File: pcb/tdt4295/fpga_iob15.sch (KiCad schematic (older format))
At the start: 18 parts

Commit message: add another capacitor :)
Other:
- note added: "Have SPIs between FPGA and MCU on IOB15?"
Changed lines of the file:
@@
 Text Notes 4300 2550 2    50   ~ 0
 Datasheet says:\n1x47uF\n2x4.7uF\n4x470nF
+Text Notes 4650 3400 2    50   ~ 10
+Have SPIs between FPGA and MCU on IOB15?
 $EndSCHEMATC

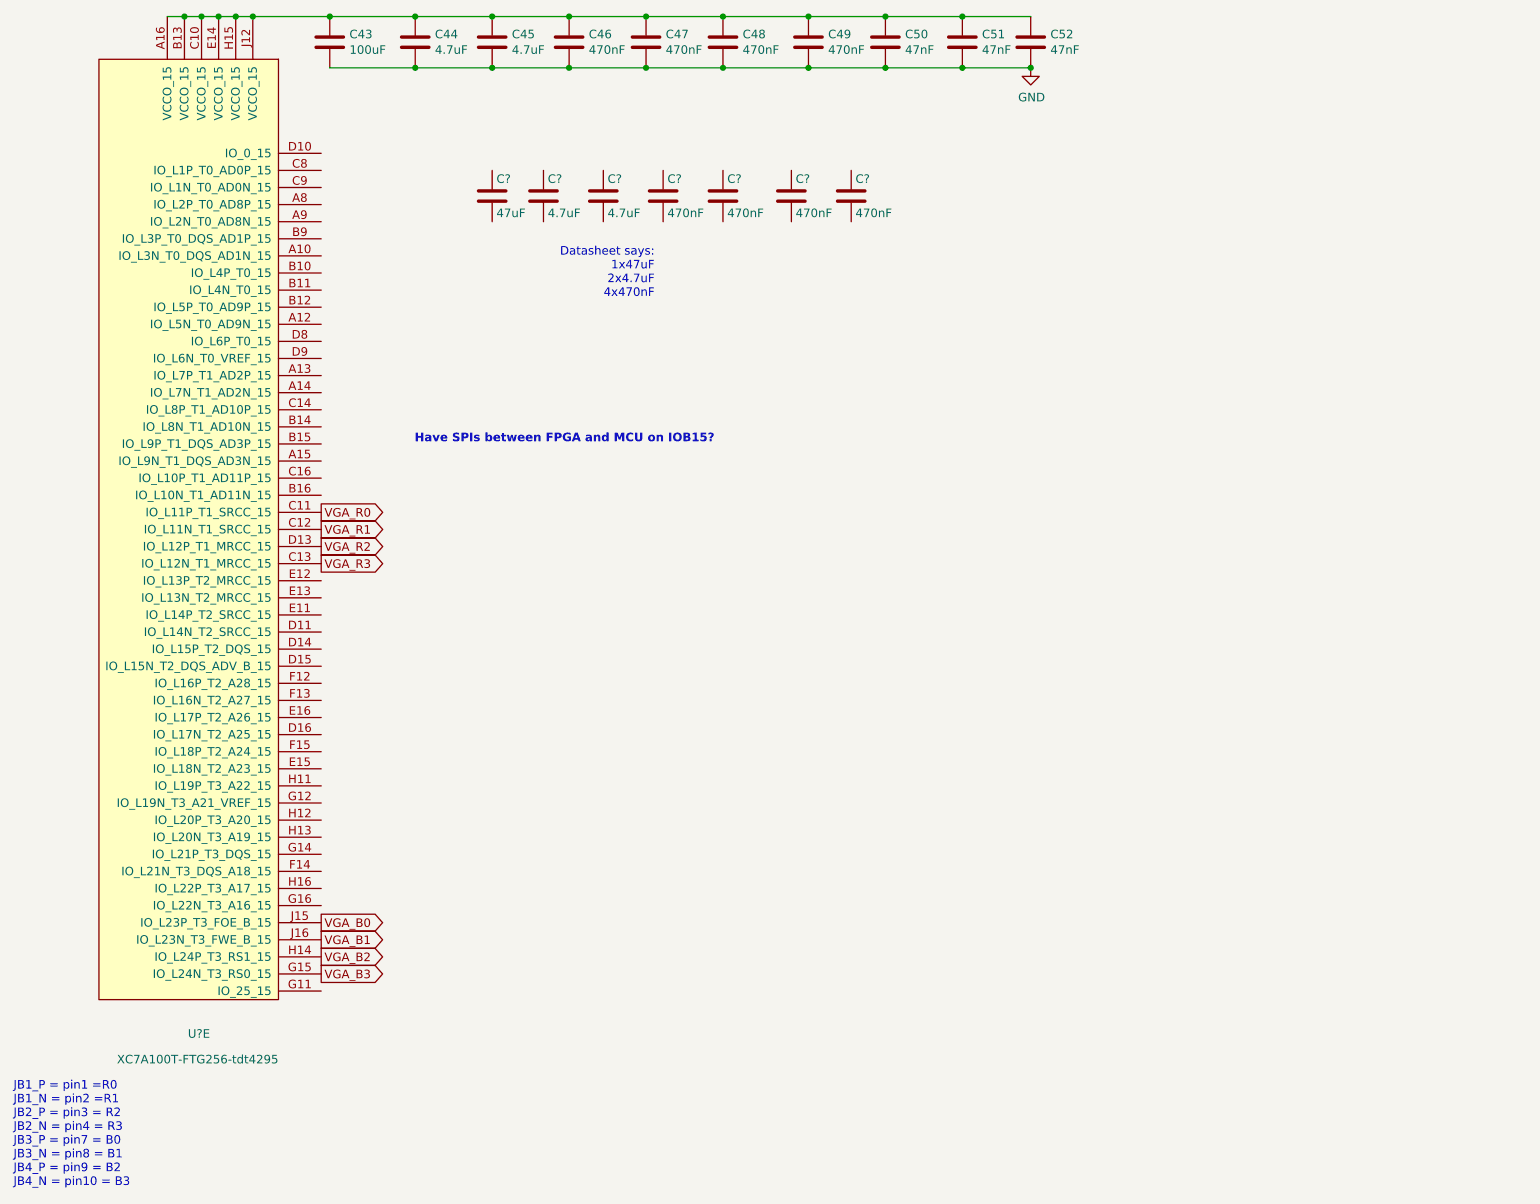
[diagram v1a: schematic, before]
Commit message: Add digikey footprints, implement (some) capacitor footprints in schematic
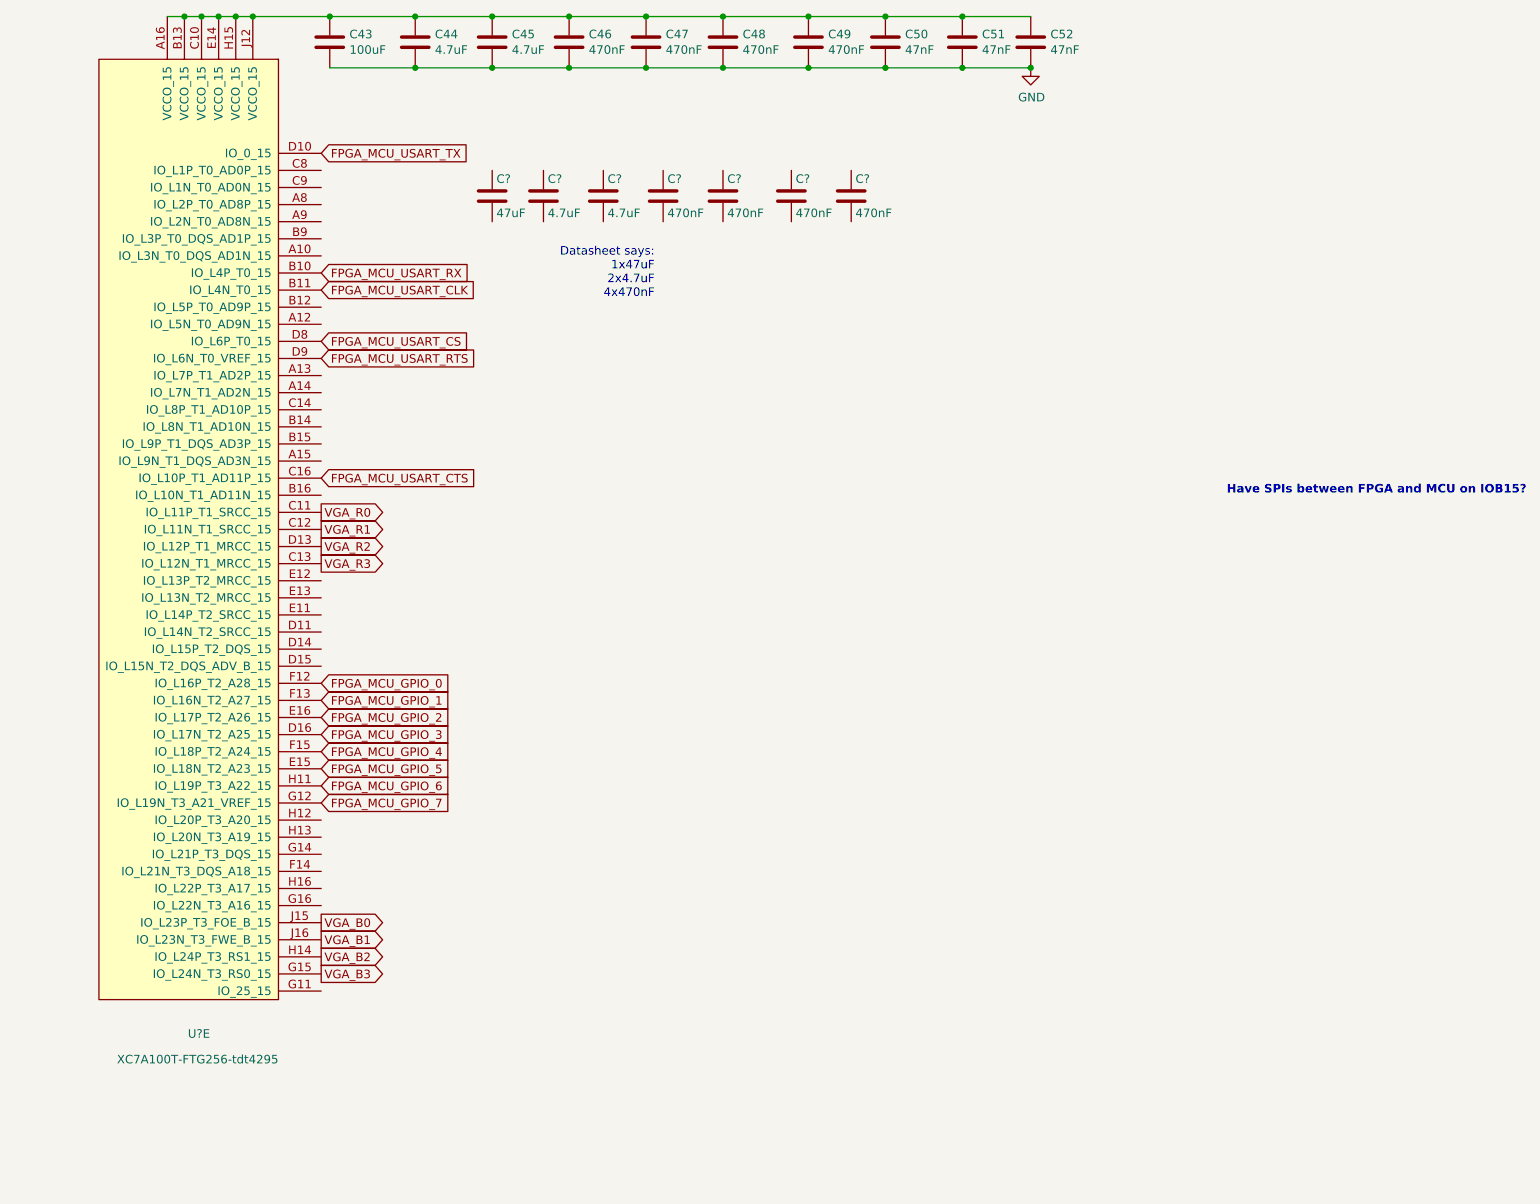
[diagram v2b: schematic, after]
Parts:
- C44, C45, C49, C? (x2): footprint (none) -> Capacitor_SMD:C_0805_2012Metric_Pad1.18x1.45mm_HandSolder
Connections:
- net FPGA_MCU_USART_RX: now reaches U?.B10 (IO_L4P_T0_15)
- net FPGA_MCU_USART_CLK: now reaches U?.B11 (IO_L4N_T0_15)
- net FPGA_MCU_USART_CTS: now reaches U?.C16 (IO_L10P_T1_AD11P_15)
- net FPGA_MCU_USART_TX: now reaches U?.D10 (IO_0_15)
- net FPGA_MCU_GPIO_3: now reaches U?.D16 (IO_L17N_T2_A25_15)
- net FPGA_MCU_USART_CS: now reaches U?.D8 (IO_L6P_T0_15)
- net FPGA_MCU_USART_RTS: now reaches U?.D9 (IO_L6N_T0_VREF_15)
- net FPGA_MCU_GPIO_5: now reaches U?.E15 (IO_L18N_T2_A23_15)
- net FPGA_MCU_GPIO_2: now reaches U?.E16 (IO_L17P_T2_A26_15)
- net FPGA_MCU_GPIO_0: now reaches U?.F12 (IO_L16P_T2_A28_15)
- net FPGA_MCU_GPIO_1: now reaches U?.F13 (IO_L16N_T2_A27_15)
- net FPGA_MCU_GPIO_4: now reaches U?.F15 (IO_L18P_T2_A24_15)
- net FPGA_MCU_GPIO_7: now reaches U?.G12 (IO_L19N_T3_A21_VREF_15)
- net FPGA_MCU_GPIO_6: now reaches U?.H11 (IO_L19P_T3_A22_15)
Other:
- note removed: "JB1_P = pin1 =R0\nJB1_N = pin2 =R1\nJB2_P = pin3 = R2\nJB2_N = pin4 = R3\nJB3_P = pin7 = B0\nJB3_N = pin8 = B1\nJB4_P = pin9 = B2\nJB4_N = pin10 = B3"
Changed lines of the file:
@@
 	1    0    0    -1
 $EndComp
-Text Notes 550  7750 0    50   ~ 0
-JB1_P = pin1 =R0\nJB1_N = pin2 =R1\nJB2_P = pin3 = R2\nJB2_N = pin4 = R3\nJB3_P = pin7 = B0\nJB3_N = pin8 = B1\nJB4_P = pin9 = B2\nJB4_N = pin10 = B3
 $Comp
 L Device:C C43
@@
 F 0 "C44" H 3015 1096 50  0000 L CNN
 F 1 "4.7uF" H 3015 1005 50  0000 L CNN
-F 2 "" H 2938 900 50  0001 C CNN
+F 2 "Capacitor_SMD:C_0805_2012Metric_Pad1.18x1.45mm_HandSolder" H 2938 900 50  0001 C CNN
 F 3 "~" H 2900 1050 50  0001 C CNN
 	1    2900 1050
@@
 F 0 "C45" H 3465 1096 50  0000 L CNN
 F 1 "4.7uF" H 3465 1005 50  0000 L CNN
-F 2 "" H 3388 900 50  0001 C CNN
+F 2 "Capacitor_SMD:C_0805_2012Metric_Pad1.18x1.45mm_HandSolder" H 3388 900 50  0001 C CNN
 F 3 "~" H 3350 1050 50  0001 C CNN
 	1    3350 1050
@@
 F 0 "C49" H 5315 1096 50  0000 L CNN
 F 1 "470nF" H 5315 1005 50  0000 L CNN
-F 2 "" H 5238 900 50  0001 C CNN
+F 2 "Capacitor_SMD:C_0805_2012Metric_Pad1.18x1.45mm_HandSolder" H 5238 900 50  0001 C CNN
 F 3 "~" H 5200 1050 50  0001 C CNN
 	1    5200 1050
@@
 F 0 "C?" H 3675 2050 50  0000 L CNN
 F 1 "4.7uF" H 3675 1850 50  0000 L CNN
-F 2 "" H 3688 1800 50  0001 C CNN
+F 2 "Capacitor_SMD:C_0805_2012Metric_Pad1.18x1.45mm_HandSolder" H 3688 1800 50  0001 C CNN
 F 3 "~" H 3650 1950 50  0001 C CNN
 	1    3650 1950
@@
 F 0 "C?" H 4025 2050 50  0000 L CNN
 F 1 "4.7uF" H 4025 1850 50  0000 L CNN
-F 2 "" H 4038 1800 50  0001 C CNN
+F 2 "Capacitor_SMD:C_0805_2012Metric_Pad1.18x1.45mm_HandSolder" H 4038 1800 50  0001 C CNN
 F 3 "~" H 4000 1950 50  0001 C CNN
 	1    4000 1950
@@
 Text Notes 4300 2550 2    50   ~ 0
 Datasheet says:\n1x47uF\n2x4.7uF\n4x470nF
-Text Notes 4650 3400 2    50   ~ 10
+Text Notes 9400 3700 2    50   ~ 10
 Have SPIs between FPGA and MCU on IOB15?
+Text GLabel 2350 1700 2    50   Input ~ 0
+FPGA_MCU_USART_TX
+Text GLabel 2350 2500 2    50   Input ~ 0
+FPGA_MCU_USART_CLK
+Text GLabel 2350 2400 2    50   Input ~ 0
+FPGA_MCU_USART_RX
+Text GLabel 2350 2800 2    50   Input ~ 0
+FPGA_MCU_USART_CS
+Text GLabel 2350 2900 2    50   Input ~ 0
+FPGA_MCU_USART_RTS
+Text GLabel 2350 3600 2    50   Input ~ 0
+FPGA_MCU_USART_CTS
+Text GLabel 2350 4800 2    50   Input ~ 0
+FPGA_MCU_GPIO_0
+Text GLabel 2350 4900 2    50   Input ~ 0
+FPGA_MCU_GPIO_1
+Text GLabel 2350 5000 2    50   Input ~ 0
+FPGA_MCU_GPIO_2
+Text GLabel 2350 5100 2    50   Input ~ 0
+FPGA_MCU_GPIO_3
+Text GLabel 2350 5200 2    50   Input ~ 0
+FPGA_MCU_GPIO_4
+Text GLabel 2350 5300 2    50   Input ~ 0
+FPGA_MCU_GPIO_5
+Text GLabel 2350 5400 2    50   Input ~ 0
+FPGA_MCU_GPIO_6
+Text GLabel 2350 5500 2    50   Input ~ 0
+FPGA_MCU_GPIO_7
 $EndSCHEMATC

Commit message: connect MCU to FPGA
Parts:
- renumbered C43 to C?, C44 to C?, C45 to C?, C46 to C?, C47 to C?, C48 to C?, C49 to C?, C50 to C?, C51 to C?, C52 to C?
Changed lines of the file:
@@
 $Descr A4 11693 8268
 encoding utf-8
-Sheet 3 5
+Sheet 5 7
 Title ""
 Date ""
@@
 $EndComp
 $Comp
-L Device:C C43
+L Device:C C?
 U 1 1 614DC8F2
 P 2400 1050
-F 0 "C43" H 2515 1096 50  0000 L CNN
+F 0 "C?" H 2515 1096 50  0000 L CNN
 F 1 "100uF" H 2515 1005 50  0000 L CNN
 F 2 "" H 2438 900 50  0001 C CNN
@@
 $EndComp
 $Comp
-L Device:C C44
+L Device:C C?
 U 1 1 614DE01C
 P 2900 1050
-F 0 "C44" H 3015 1096 50  0000 L CNN
+F 0 "C?" H 3015 1096 50  0000 L CNN
 F 1 "4.7uF" H 3015 1005 50  0000 L CNN
 F 2 "Capacitor_SMD:C_0805_2012Metric_Pad1.18x1.45mm_HandSolder" H 2938 900 50  0001 C CNN
@@
 $EndComp
 $Comp
-L Device:C C45
+L Device:C C?
 U 1 1 614DE58E
 P 3350 1050
-F 0 "C45" H 3465 1096 50  0000 L CNN
+F 0 "C?" H 3465 1096 50  0000 L CNN
 F 1 "4.7uF" H 3465 1005 50  0000 L CNN
 F 2 "Capacitor_SMD:C_0805_2012Metric_Pad1.18x1.45mm_HandSolder" H 3388 900 50  0001 C CNN
@@
 $EndComp
 $Comp
-L Device:C C46
+L Device:C C?
 U 1 1 614DEA18
 P 3800 1050
-F 0 "C46" H 3915 1096 50  0000 L CNN
+F 0 "C?" H 3915 1096 50  0000 L CNN
 F 1 "470nF" H 3915 1005 50  0000 L CNN
 F 2 "" H 3838 900 50  0001 C CNN
@@
 $EndComp
 $Comp
-L Device:C C47
+L Device:C C?
 U 1 1 614DF153
 P 4250 1050
-F 0 "C47" H 4365 1096 50  0000 L CNN
+F 0 "C?" H 4365 1096 50  0000 L CNN
 F 1 "470nF" H 4365 1005 50  0000 L CNN
 F 2 "" H 4288 900 50  0001 C CNN
@@
 $EndComp
 $Comp
-L Device:C C48
+L Device:C C?
 U 1 1 614DF5FE
 P 4700 1050
-F 0 "C48" H 4815 1096 50  0000 L CNN
+F 0 "C?" H 4815 1096 50  0000 L CNN
 F 1 "470nF" H 4815 1005 50  0000 L CNN
 F 2 "" H 4738 900 50  0001 C CNN
@@
 $EndComp
 $Comp
-L Device:C C49
+L Device:C C?
 U 1 1 614DFBD9
 P 5200 1050
-F 0 "C49" H 5315 1096 50  0000 L CNN
+F 0 "C?" H 5315 1096 50  0000 L CNN
 F 1 "470nF" H 5315 1005 50  0000 L CNN
 F 2 "Capacitor_SMD:C_0805_2012Metric_Pad1.18x1.45mm_HandSolder" H 5238 900 50  0001 C CNN
@@
 $EndComp
 $Comp
-L Device:C C50
+L Device:C C?
 U 1 1 614E00E6
 P 5650 1050
-F 0 "C50" H 5765 1096 50  0000 L CNN
+F 0 "C?" H 5765 1096 50  0000 L CNN
 F 1 "47nF" H 5765 1005 50  0000 L CNN
 F 2 "" H 5688 900 50  0001 C CNN
@@
 $EndComp
 $Comp
-L Device:C C51
+L Device:C C?
 U 1 1 614E08F1
 P 6100 1050
-F 0 "C51" H 6215 1096 50  0000 L CNN
+F 0 "C?" H 6215 1096 50  0000 L CNN
 F 1 "47nF" H 6215 1005 50  0000 L CNN
 F 2 "" H 6138 900 50  0001 C CNN
@@
 $EndComp
 $Comp
-L Device:C C52
+L Device:C C?
 U 1 1 614E0EB5
 P 6500 1050
-F 0 "C52" H 6615 1096 50  0000 L CNN
+F 0 "C?" H 6615 1096 50  0000 L CNN
 F 1 "47nF" H 6615 1005 50  0000 L CNN
 F 2 "" H 6538 900 50  0001 C CNN
@@
 AR Path="/61459CB7/615F1C9B" Ref="C?"  Part="1"
 AR Path="/614933B1/615F1C9B" Ref="C?"  Part="1"
+AR Path="/617F72AC/614933B1/615F1C9B" Ref="C?"  Part="1"
 F 0 "C?" H 3375 2050 50  0000 L CNN
 F 1 "47uF" H 3375 1850 50  0000 L CNN
@@
 AR Path="/61459CB7/615F1CA1" Ref="C?"  Part="1"
 AR Path="/614933B1/615F1CA1" Ref="C?"  Part="1"
+AR Path="/617F72AC/614933B1/615F1CA1" Ref="C?"  Part="1"
 F 0 "C?" H 3675 2050 50  0000 L CNN
 F 1 "4.7uF" H 3675 1850 50  0000 L CNN
@@
 AR Path="/61459CB7/615F1CA7" Ref="C?"  Part="1"
 AR Path="/614933B1/615F1CA7" Ref="C?"  Part="1"
+AR Path="/617F72AC/614933B1/615F1CA7" Ref="C?"  Part="1"
 F 0 "C?" H 4025 2050 50  0000 L CNN
 F 1 "4.7uF" H 4025 1850 50  0000 L CNN
@@
 AR Path="/61459CB7/615F1CAD" Ref="C?"  Part="1"
 AR Path="/614933B1/615F1CAD" Ref="C?"  Part="1"
+AR Path="/617F72AC/614933B1/615F1CAD" Ref="C?"  Part="1"
 F 0 "C?" H 4375 2050 50  0000 L CNN
 F 1 "470nF" H 4375 1850 50  0000 L CNN
@@
 AR Path="/61459CB7/615F1CB3" Ref="C?"  Part="1"
 AR Path="/614933B1/615F1CB3" Ref="C?"  Part="1"
+AR Path="/617F72AC/614933B1/615F1CB3" Ref="C?"  Part="1"
 F 0 "C?" H 4725 2050 50  0000 L CNN
 F 1 "470nF" H 4725 1850 50  0000 L CNN
@@
 AR Path="/61459CB7/615F1CB9" Ref="C?"  Part="1"
 AR Path="/614933B1/615F1CB9" Ref="C?"  Part="1"
+AR Path="/617F72AC/614933B1/615F1CB9" Ref="C?"  Part="1"
 F 0 "C?" H 5125 2050 50  0000 L CNN
 F 1 "470nF" H 5125 1850 50  0000 L CNN
@@
 AR Path="/61459CB7/615F1CBF" Ref="C?"  Part="1"
 AR Path="/614933B1/615F1CBF" Ref="C?"  Part="1"
+AR Path="/617F72AC/614933B1/615F1CBF" Ref="C?"  Part="1"
 F 0 "C?" H 5475 2050 50  0000 L CNN
 F 1 "470nF" H 5475 1850 50  0000 L CNN
